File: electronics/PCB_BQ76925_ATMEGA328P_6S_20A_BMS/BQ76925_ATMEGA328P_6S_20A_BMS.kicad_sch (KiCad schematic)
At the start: 9 parts, among them Q1 IRFB4110, U1 BQ76925PW, U2 ATmega328P-A, U3 AMS1117-5.0

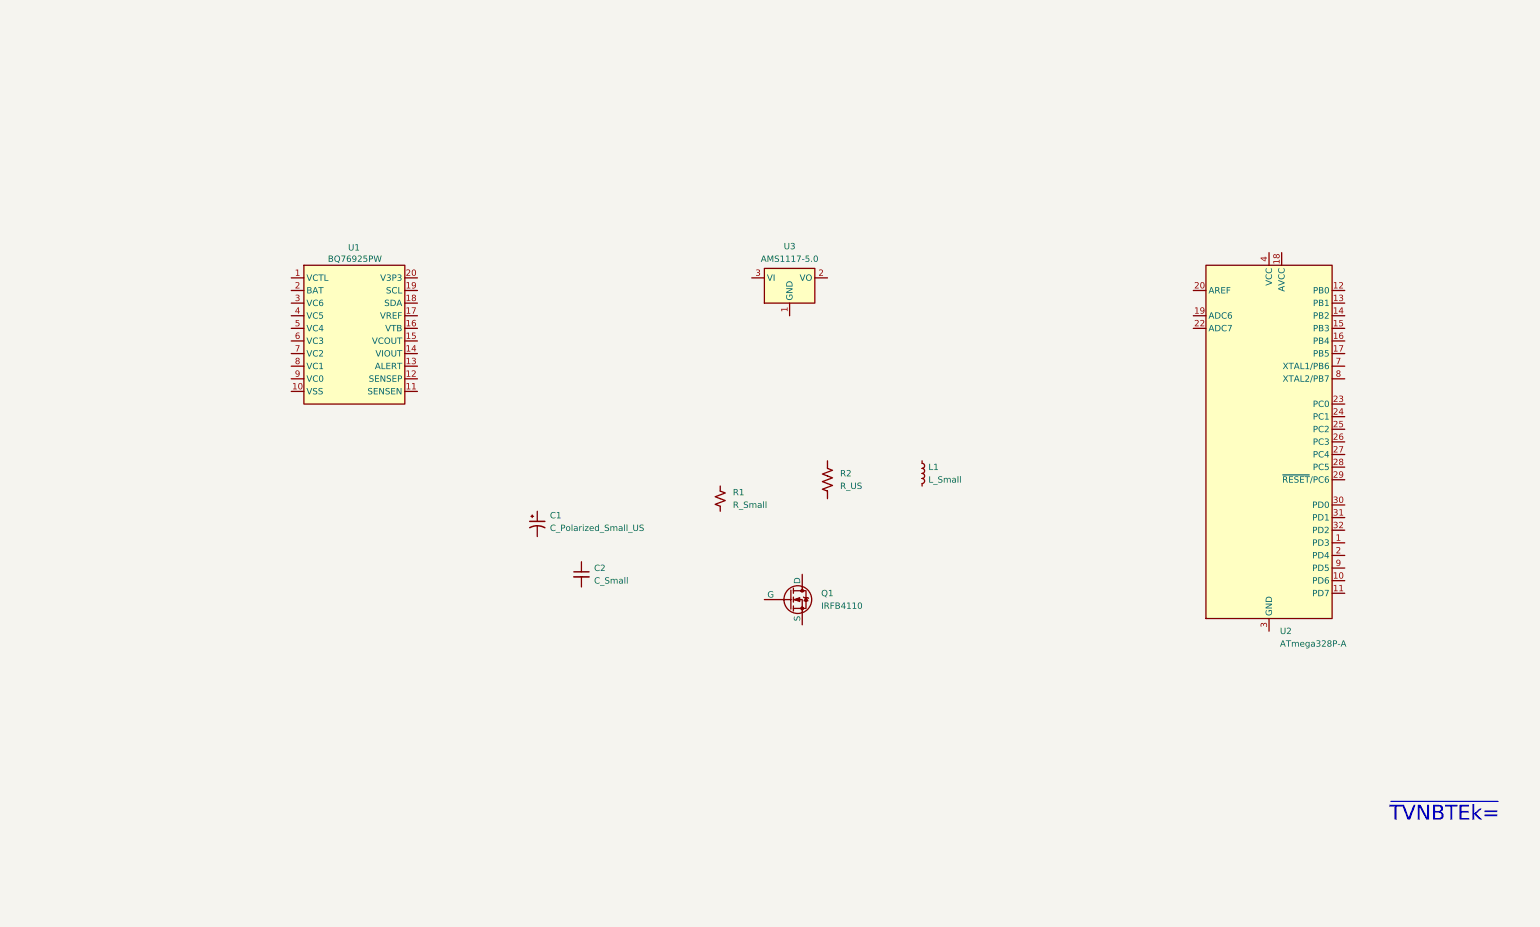
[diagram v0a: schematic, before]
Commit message: schematic progress completed AFE, made schematic structure
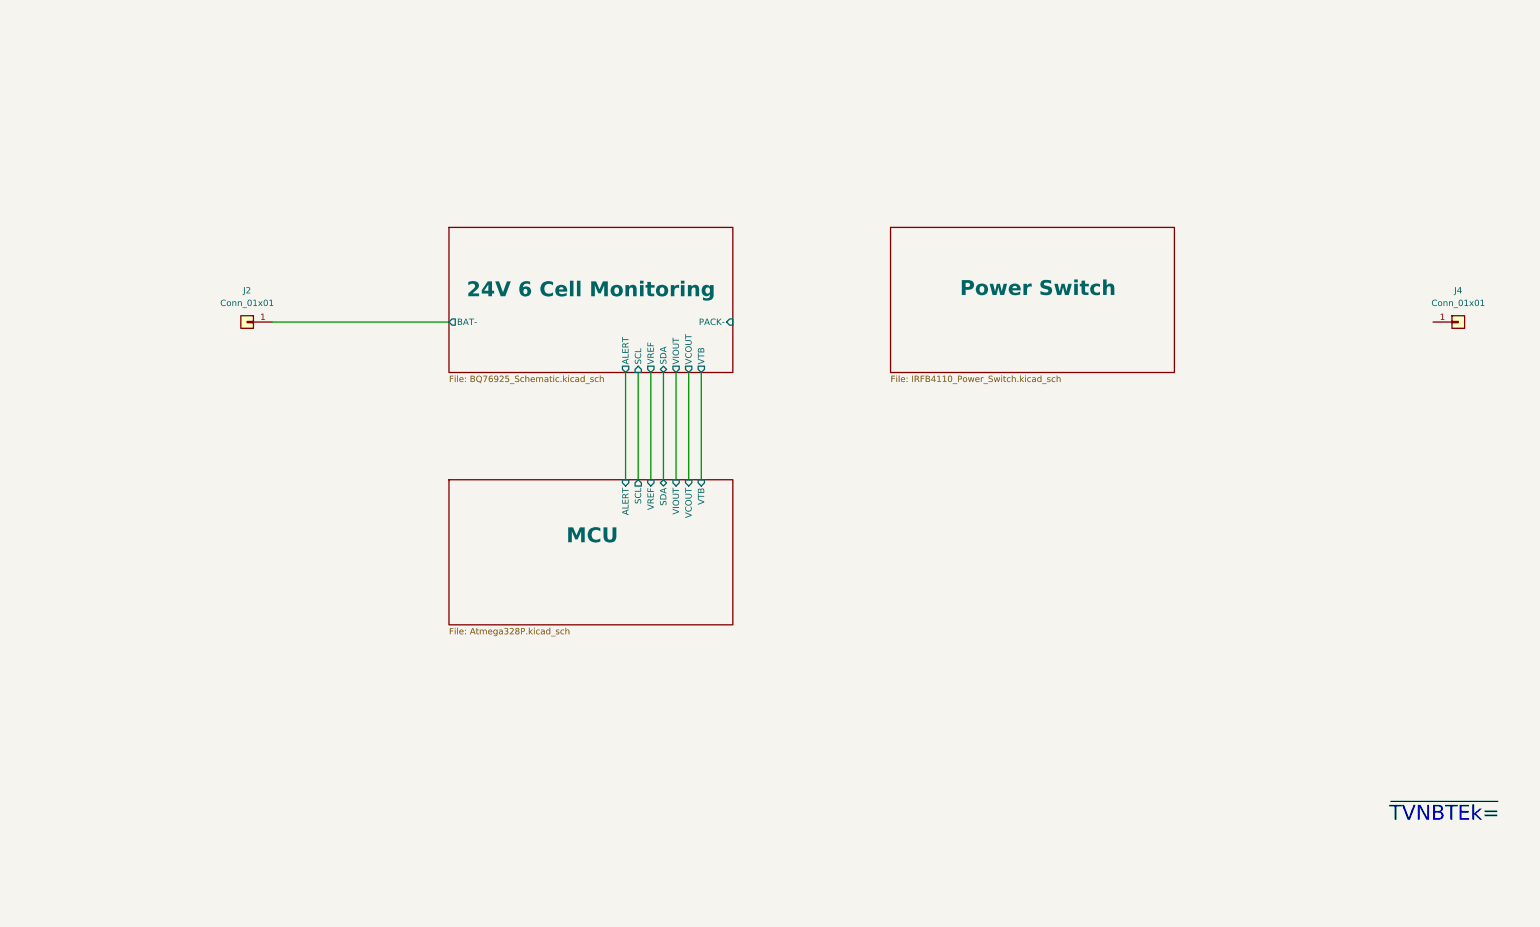
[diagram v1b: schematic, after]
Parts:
- removed C1: C_Polarized_Small_US, symbol BQ76925_ATMEGA328P_6S_20A_BMS:C_Polarized_Small_US
- removed C2: C_Small, symbol BQ76925_ATMEGA328P_6S_20A_BMS:C_Small
- removed L1: L_Small, symbol BQ76925_ATMEGA328P_6S_20A_BMS:L_Small
- removed Q1: IRFB4110, Package_TO_SOT_THT:TO-220-3_Horizontal_TabDown, symbol BQ76925_ATMEGA328P_6S_20A_BMS:IRFB4110
- removed R1: R_Small, symbol BQ76925_ATMEGA328P_6S_20A_BMS:R_Small_US
- removed R2: R_US, symbol BQ76925_ATMEGA328P_6S_20A_BMS:R_US
- removed U1: BQ76925PW, Package_SO:TSSOP-20_4.4x6.5mm_P0.65mm, symbol BQ76925_ATMEGA328P_6S_20A_BMS:BQ76925PW
- removed U2: ATmega328P-A, Package_QFP:TQFP-32_7x7mm_P0.8mm, symbol BQ76925_ATMEGA328P_6S_20A_BMS:ATmega328P-A
- removed U3: AMS1117-5.0, Package_TO_SOT_SMD:SOT-223-3_TabPin2, symbol BQ76925_ATMEGA328P_6S_20A_BMS:AMS1117-5.0
- added J2, J4: Conn_01x01, symbol BQ76925_ATMEGA328P_6S_20A_BMS:Conn_01x01
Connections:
- new net 24V 6 Cell Monitoring/BAT-: J2.1 (Pin_1)
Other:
- added sheet 24V 6 Cell Monitoring (BQ76925_Schematic.kicad_sch)
- added sheet MCU (Atmega328P.kicad_sch)
- added sheet Power Switch (IRFB4110_Power_Switch.kicad_sch)

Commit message: schematic completed component need to be finalised
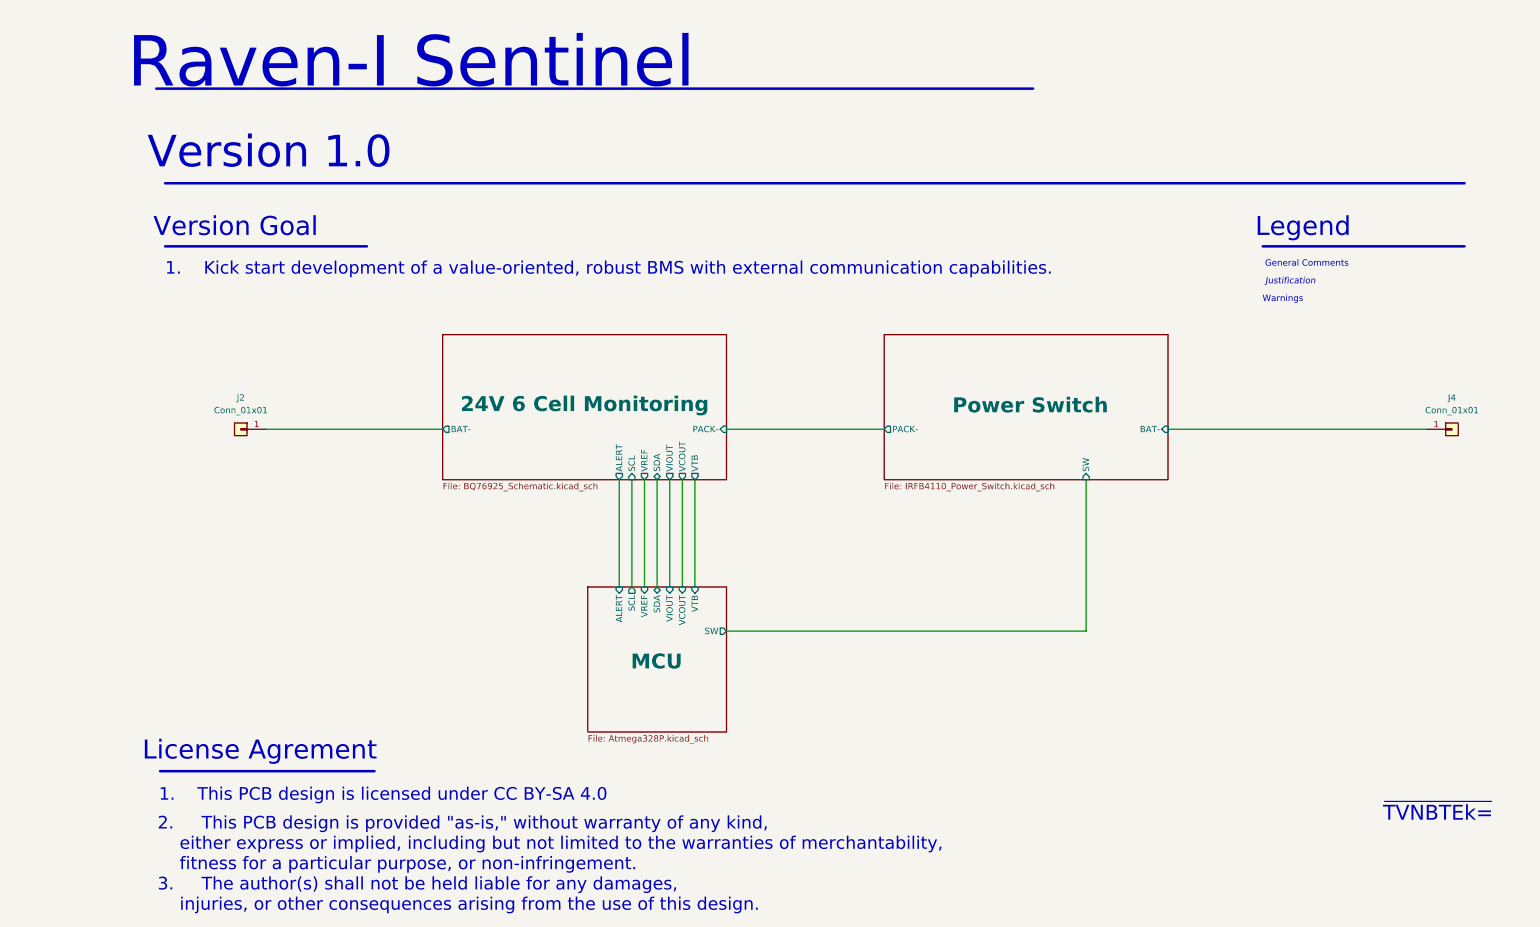
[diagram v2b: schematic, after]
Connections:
- net Power Switch/BAT-: now reaches J4.1 (Pin_1)
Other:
- sheet MCU ports: added SW; removed none
- sheet Power Switch ports: added BAT-, PACK-, SW; removed none
- note added: "1. Kick start development of a value-oriented, robust BMS with external communication capabilities."
- note added: "1. This PCB design is licensed under CC BY-SA 4.0"
- note added: "2. This PCB design is provided "as-is," without warranty of any kind, either express or implied, including but not limited to the warranties of merchantability, fitness for a particular purpose, or non-infringement. 3. The author(s) shall not be held liable for any damages, injuries, or other consequences arising from the use of this design."
- note added: "General Comments"
- note added: "Justification"
- note added: "Legend"
- note added: "License Agrement"
- note added: "Raven-I Sentinel"
- note added: "Version ${REVISION}"
- note added: "Version Goal"
- note added: "Warnings"
- moved on the sheet: J2, J4

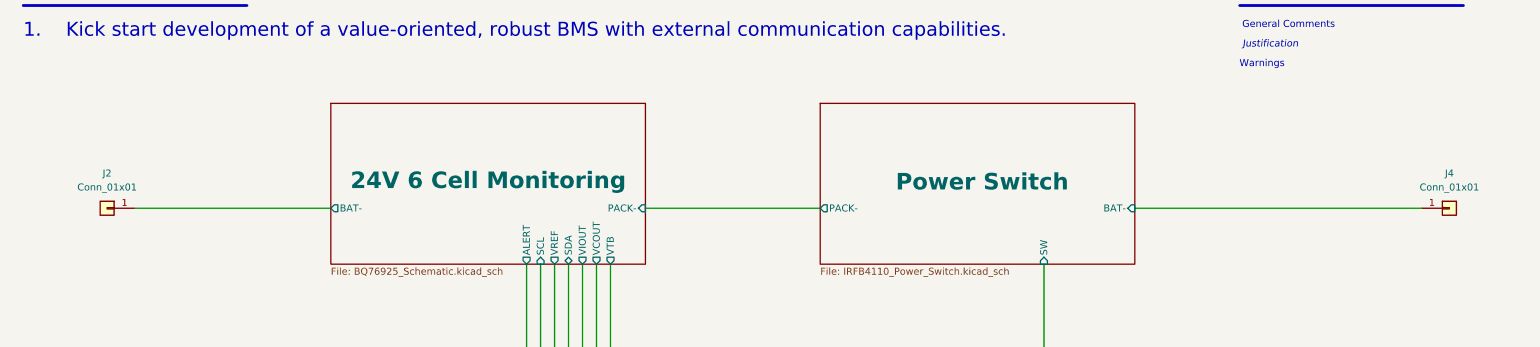
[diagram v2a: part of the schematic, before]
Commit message: Schematic completed components calculated need to check avaialability
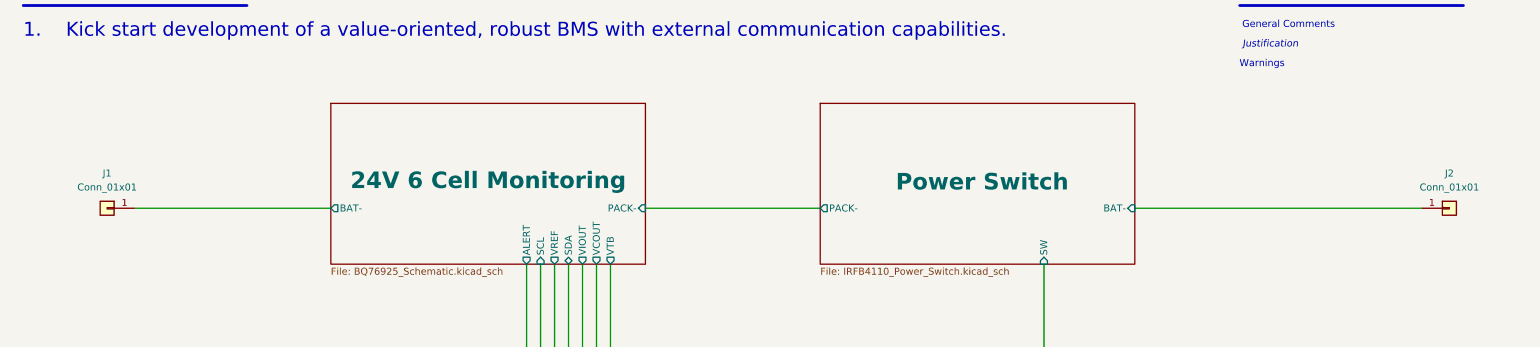
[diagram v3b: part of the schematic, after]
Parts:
- renumbered J2 to J1, J4 to J2
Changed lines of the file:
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@@
 	(title_block
 		(title "Raven-I Sentinel")
+		(date "2024-11-23")
 		(rev "1.0")
 		(company "M S Ali")
@@
 		(dnp no)
 		(fields_autoplaced yes)
-		(property "Reference" "J2"
+		(property "Reference" "J1"
 			(at 30.48 91.44 0)
 			(effects
@@
 		(property "Description" "Generic connector, single row, 01x01, script generated (kicad-library-utils/schlib/autogen/connector/)"
 			(at 30.48 97.79 0)
+			(effects
+				(font
+					(size 1.27 1.27)
+				)
+				(hide yes)
+			)
+		)
+		(pin "1"
+		)
+		(instances
+			(project "BQ76925_ATMEGA328P_6S_20A_BMS"
+				(path "/624a087f-322b-4a70-8c29-0e4f8f018e16"
+					(reference "J1")
+					(unit 1)
+				)
+			)
+		)
+	)
+	(symbol
+		(lib_id "BQ76925_ATMEGA328P_6S_20A_BMS:Conn_01x01")
+		(at 274.32 97.79 0)
+		(unit 1)
+		(exclude_from_sim no)
+		(in_bom yes)
+		(on_board yes)
+		(dnp no)
+		(property "Reference" "J2"
+			(at 274.32 91.44 0)
+			(effects
+				(font
+					(size 1.27 1.27)
+				)
+			)
+		)
+		(property "Value" "Conn_01x01"
+			(at 274.32 93.98 0)
+			(effects
+				(font
+					(size 1.27 1.27)
+				)
+			)
+		)
+		(property "Footprint" ""
+			(at 274.32 97.79 0)
+			(effects
+				(font
+					(size 1.27 1.27)
+				)
+				(hide yes)
+			)
+		)
+		(property "Datasheet" "~"
+			(at 274.32 97.79 0)
+			(effects
+				(font
+					(size 1.27 1.27)
+				)
+				(hide yes)
+			)
+		)
+		(property "Description" "Generic connector, single row, 01x01, script generated (kicad-library-utils/schlib/autogen/connector/)"
+			(at 274.32 97.79 0)
 			(effects
 				(font
@@
 					(unit 1)
 				)
-			)
-		)
-	)
-	(symbol
-		(lib_id "BQ76925_ATMEGA328P_6S_20A_BMS:Conn_01x01")
-		(at 274.32 97.79 0)
-		(unit 1)
-		(exclude_from_sim no)
-		(in_bom yes)
-		(on_board yes)
-		(dnp no)
-		(property "Reference" "J4"
-			(at 274.32 91.44 0)
-			(effects
-				(font
-					(size 1.27 1.27)
-				)
-			)
-		)
-		(property "Value" "Conn_01x01"
-			(at 274.32 93.98 0)
-			(effects
-				(font
-					(size 1.27 1.27)
-				)
-			)
-		)
-		(property "Footprint" ""
-			(at 274.32 97.79 0)
-			(effects
-				(font
-					(size 1.27 1.27)
-				)
-				(hide yes)
-			)
-		)
-		(property "Datasheet" "~"
-			(at 274.32 97.79 0)
-			(effects
-				(font
-					(size 1.27 1.27)
-				)
-				(hide yes)
-			)
-		)
-		(property "Description" "Generic connector, single row, 01x01, script generated (kicad-library-utils/schlib/autogen/connector/)"
-			(at 274.32 97.79 0)
-			(effects
-				(font
-					(size 1.27 1.27)
-				)
-				(hide yes)
-			)
-		)
-		(pin "1"
-		)
-		(instances
-			(project "BQ76925_ATMEGA328P_6S_20A_BMS"
-				(path "/624a087f-322b-4a70-8c29-0e4f8f018e16"
-					(reference "J4")
-					(unit 1)
-				)

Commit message: schematic components footprint updated
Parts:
- J1, J2: footprint (none) -> Connector_Wire:SolderWirePad_1x01_SMD_5x10mm
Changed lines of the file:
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@@
 			)
 		)
-		(property "Footprint" ""
+		(property "Footprint" "Connector_Wire:SolderWirePad_1x01_SMD_5x10mm"
 			(at 30.48 97.79 0)
 			(effects
@@
 			)
 		)
-		(property "Footprint" ""
+		(property "Footprint" "Connector_Wire:SolderWirePad_1x01_SMD_5x10mm"
 			(at 274.32 97.79 0)
 			(effects

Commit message: pcb design half complete
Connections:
- net Power Switch/BAT- renamed Power Switch/PACK-
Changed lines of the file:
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@@
 		)
 		(pin "PACK-" output
+			(at 217.17 97.79 0)
+			(effects
+				(font
+					(size 1.27 1.27)
+				)
+				(justify right)
+			)
+		)
+		(pin "BAT-" input
 			(at 160.02 97.79 180)
 			(effects
@@
 			)
 		)
-		(pin "BAT-" input
-			(at 217.17 97.79 0)
-			(effects
-				(font
-					(size 1.27 1.27)
-				)
-				(justify right)
-			)
-		)

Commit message: PCB DRC complete footprints library exported. PCB optimization required
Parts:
- J1, J2: footprint Connector_Wire:SolderWirePad_1x01_SMD_5x10mm -> BQ76925_ATMEGA328P_6S_20A_BMS:SolderWirePad_1x01_SMD_5x10mm
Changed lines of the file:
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@@
 			)
 		)
-		(property "Footprint" "Connector_Wire:SolderWirePad_1x01_SMD_5x10mm"
+		(property "Footprint" "BQ76925_ATMEGA328P_6S_20A_BMS:SolderWirePad_1x01_SMD_5x10mm"
 			(at 30.48 97.79 0)
 			(effects
@@
 			)
 		)
-		(property "Footprint" "Connector_Wire:SolderWirePad_1x01_SMD_5x10mm"
+		(property "Footprint" "BQ76925_ATMEGA328P_6S_20A_BMS:SolderWirePad_1x01_SMD_5x10mm"
 			(at 274.32 97.79 0)
 			(effects
